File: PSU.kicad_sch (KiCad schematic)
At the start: 34 parts

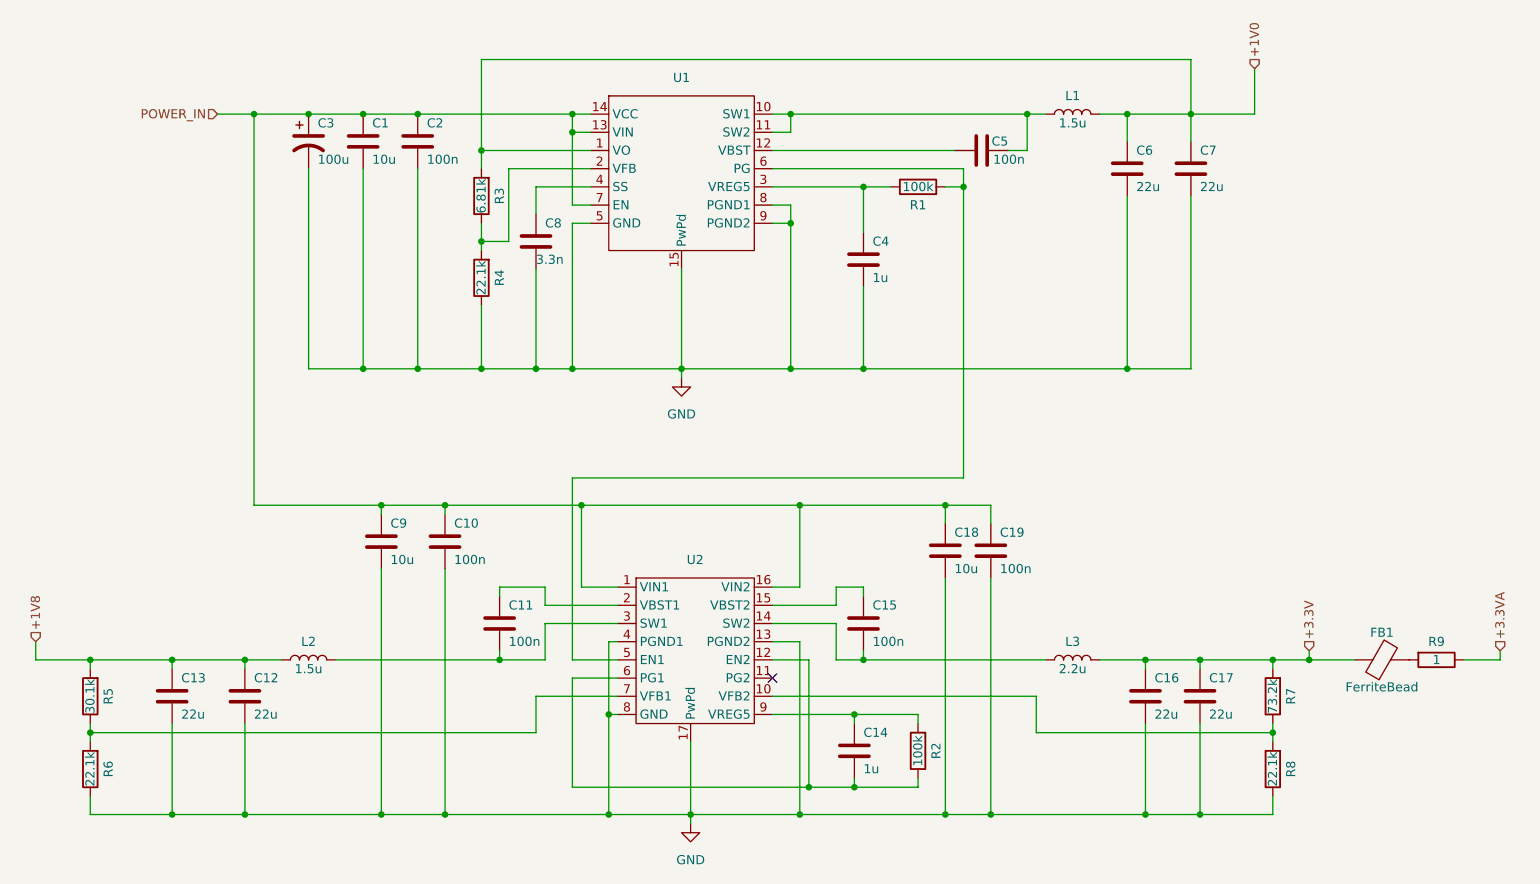
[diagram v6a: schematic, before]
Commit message: Added output pins from PSU schematic
Also renamed FPGA decoupler circuit to not have a typo
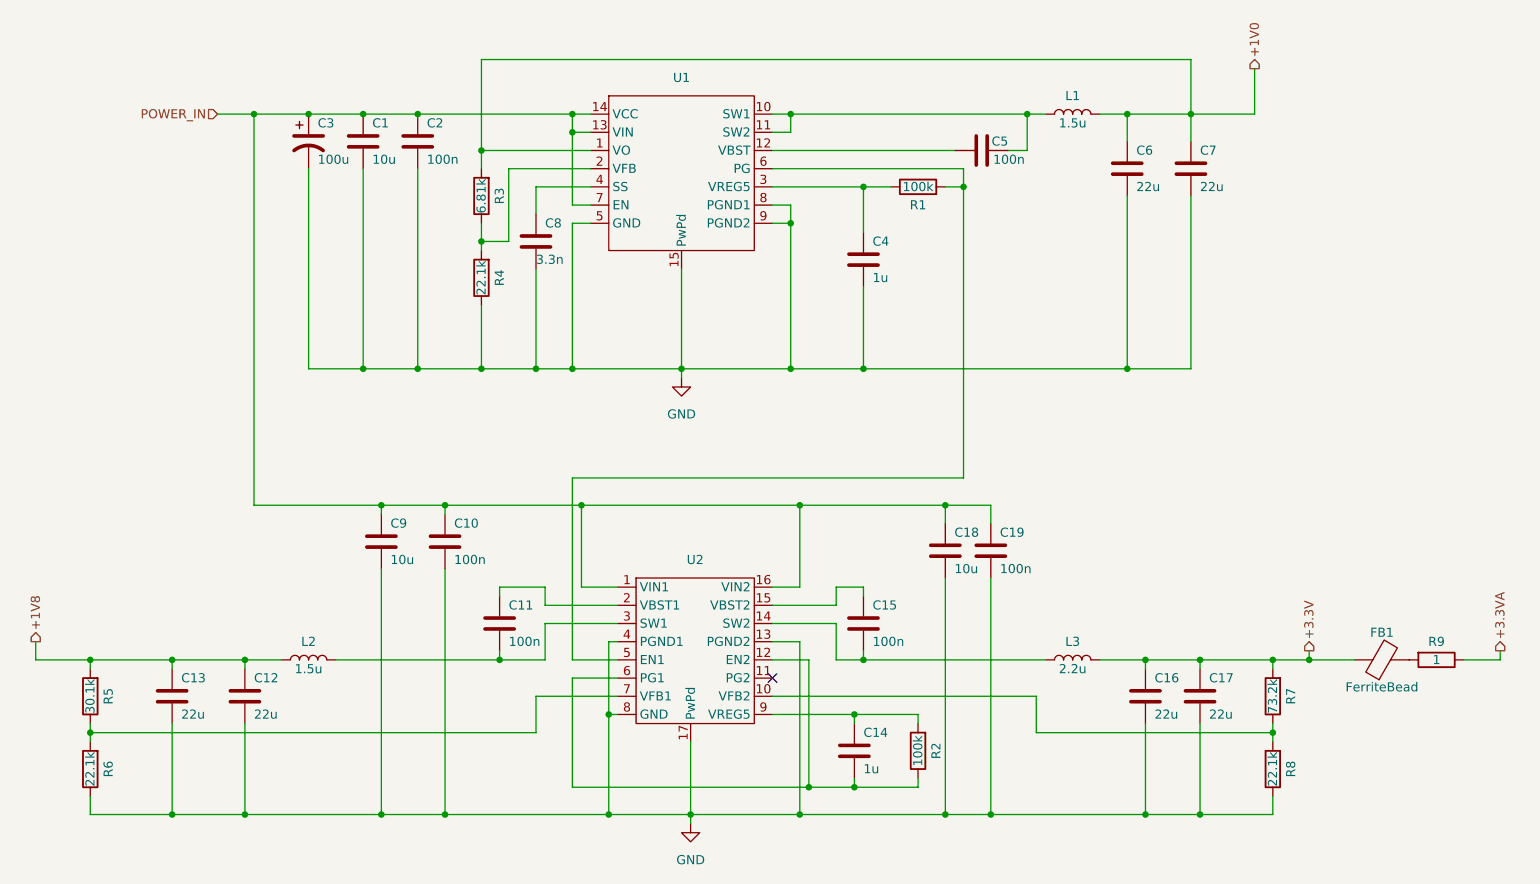
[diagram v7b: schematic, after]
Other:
- title: (none) -> Power Supply Unit
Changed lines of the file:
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@@
 (kicad_sch (version 20230121) (generator eeschema)
   (paper "A4")
+  (title_block
+    (title "Power Supply Unit")
+    (date "2023-09-11")
+    (rev "0")
+  )
   (junction (at 201.93 54.61) (diameter 0) (color 0 0 0 0)
   )
@@
     (stroke (width 0) (type default))
   )
-  (hierarchical_label "+3.3V" (shape input) (at 241.3 129.54 90) (fields_autoplaced)
+  (hierarchical_label "+3.3V" (shape output) (at 241.3 129.54 90) (fields_autoplaced)
     (effects (font (size 1.27 1.27)) (justify left))
   )
-  (hierarchical_label "+1V8" (shape input) (at 63.5 128.27 90) (fields_autoplaced)
+  (hierarchical_label "+1V8" (shape output) (at 63.5 128.27 90) (fields_autoplaced)
     (effects (font (size 1.27 1.27)) (justify left))
   )
@@
     )
   )
-  (hierarchical_label "+3.3VA" (shape input) (at 267.97 129.54 90) (fields_autoplaced)
+  (hierarchical_label "+3.3VA" (shape output) (at 267.97 129.54 90) (fields_autoplaced)
     (effects (font (size 1.27 1.27)) (justify left))
   )
-  (hierarchical_label "+1V0" (shape input) (at 233.68 48.26 90) (fields_autoplaced)
+  (hierarchical_label "+1V0" (shape output) (at 233.68 48.26 90) (fields_autoplaced)
     (effects (font (size 1.27 1.27)) (justify left))
   )
